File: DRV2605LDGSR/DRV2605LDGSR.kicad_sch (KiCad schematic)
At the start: 3 parts, among them J1 Conn_01x05_Female, J2 Conn_01x05_Female, U1 DRV2605LDGSR

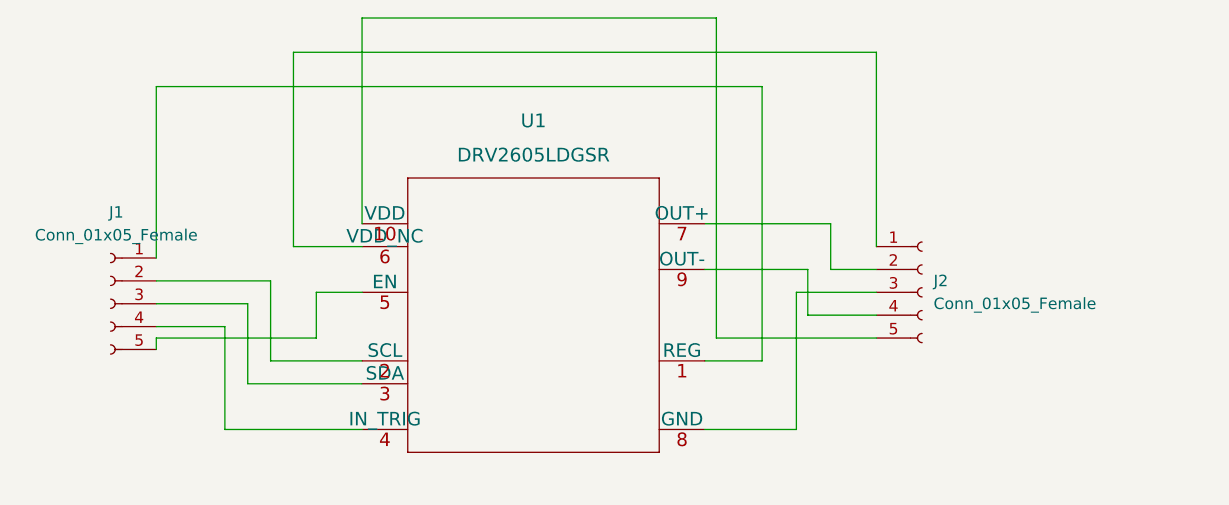
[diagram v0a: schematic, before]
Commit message: New breakout started, ADS1219, because th ADS112C04 is out of stock everywhere
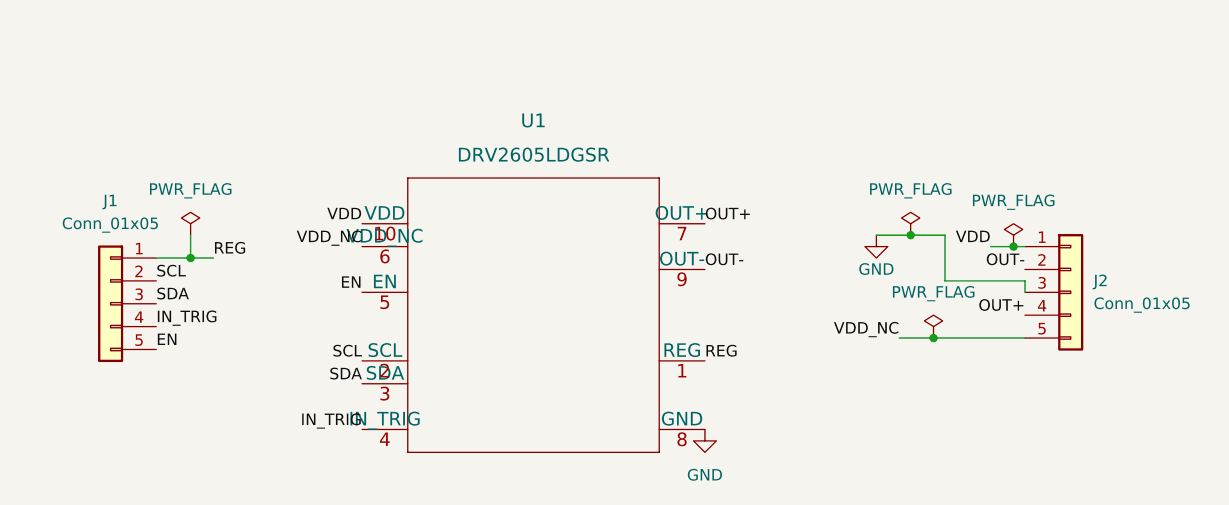
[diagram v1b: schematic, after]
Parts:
- removed J1, J2: Conn_01x05_Female, Connector_PinHeader_2.54mm:PinHeader_1x05_P2.54mm_Vertical, symbol Connector:Conn_01x05_Female
- added J1, J2: Conn_01x05, Connector_PinHeader_2.54mm:PinHeader_1x05_P2.54mm_Vertical, symbol Connector_Generic:Conn_01x05
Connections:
- net REG: now reaches U1.1 (REG)
- net REG: now also J1.1 (Pin_1)
- net SCL: now reaches U1.2 (SCL)
- net SCL: now also J1.2 (Pin_2)
- net SDA: now reaches U1.3 (SDA)
- net SDA: now also J1.3 (Pin_3)
- net IN_TRIG: now reaches U1.4 (IN_TRIG)
- net IN_TRIG: now also J1.4 (Pin_4)
- net EN: now reaches U1.5 (EN)
- net EN: now also J1.5 (Pin_5)
- net VDD: now reaches U1.10 (VDD)
- net VDD: now also J2.1 (Pin_1)
- net VDD_NC: now reaches U1.6 (VDD_NC)
- net VDD_NC: now also J2.5 (Pin_5)
- net OUT+: now reaches U1.7 (OUT+)
- net OUT+: now also J2.4 (Pin_4)
- net GND: now reaches U1.8 (GND)
- net GND: now also J2.3 (Pin_3)
- net OUT-: now reaches U1.9 (OUT-)
- net OUT-: now also J2.2 (Pin_2)
